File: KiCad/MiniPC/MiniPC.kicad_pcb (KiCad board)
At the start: 2 copper layers, 65 x 30 mm, 5 parts, among them J1 GPIO

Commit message: KiCad 15.05
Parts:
- added C2: 10u, Capacitor_THT:CP_Radial_D5.0mm_P2.00mm, B.Cu at (352.9, 88.5)
- added C3: 100n, Capacitor_THT:C_Disc_D3.0mm_W1.6mm_P2.50mm, B.Cu at (304.3, 57.0)
- added C4: 100n, Capacitor_THT:C_Disc_D3.0mm_W1.6mm_P2.50mm, B.Cu at (304.3, 60.2)
- added C5: 100n, Capacitor_THT:C_Disc_D3.0mm_W1.6mm_P2.50mm, B.Cu at (304.3, 63.4)
- added C6: 100n, Capacitor_THT:C_Disc_D3.0mm_W1.6mm_P2.50mm, B.Cu at (304.3, 66.5)
- added D1: 1N914, Diode_THT:D_DO-41_SOD81_P7.62mm_Horizontal, B.Cu at (376.7, 57.6)
- added D10: 1N914, Diode_THT:D_DO-41_SOD81_P7.62mm_Horizontal, B.Cu at (365.4, 66.1)
- added D11: 1N914, Diode_THT:D_DO-41_SOD81_P7.62mm_Horizontal, B.Cu at (365.4, 70.3)
- added D12: 1N914, Diode_THT:D_DO-41_SOD81_P7.62mm_Horizontal, B.Cu at (365.4, 74.6)
- added D13: 1N914, Diode_THT:D_DO-41_SOD81_P7.62mm_Horizontal, B.Cu at (365.4, 78.8)
- added D14: 1N914, Diode_THT:D_DO-41_SOD81_P7.62mm_Horizontal, B.Cu at (365.4, 83.1)
- added D15: 1N914, Diode_THT:D_DO-41_SOD81_P7.62mm_Horizontal, B.Cu at (354.0, 57.6)
- added D16: 1N914, Diode_THT:D_DO-41_SOD81_P7.62mm_Horizontal, B.Cu at (354.0, 61.9)
- added D17: 1N914, Diode_THT:D_DO-41_SOD81_P7.62mm_Horizontal, B.Cu at (354.0, 66.1)
- added D18: 1N914, Diode_THT:D_DO-41_SOD81_P7.62mm_Horizontal, B.Cu at (354.0, 70.3)
- added D19: 1N914, Diode_THT:D_DO-41_SOD81_P7.62mm_Horizontal, B.Cu at (354.0, 74.6)
- added D2: 1N914, Diode_THT:D_DO-41_SOD81_P7.62mm_Horizontal, B.Cu at (376.7, 61.9)
- added D20: 1N914, Diode_THT:D_DO-41_SOD81_P7.62mm_Horizontal, B.Cu at (354.0, 78.8)
- added D21: 1N914, Diode_THT:D_DO-41_SOD81_P7.62mm_Horizontal, B.Cu at (354.0, 83.1)
- added D22: 1N914, Diode_THT:D_DO-35_SOD27_P7.62mm_Horizontal, B.Cu at (377.0, 87.0)
- added D3: 1N914, Diode_THT:D_DO-41_SOD81_P7.62mm_Horizontal, B.Cu at (376.7, 66.1)
- added D4: 1N914, Diode_THT:D_DO-41_SOD81_P7.62mm_Horizontal, B.Cu at (376.7, 70.3)
- added D5: 1N914, Diode_THT:D_DO-41_SOD81_P7.62mm_Horizontal, B.Cu at (376.7, 74.6)
- added D6: 1N914, Diode_THT:D_DO-41_SOD81_P7.62mm_Horizontal, B.Cu at (376.7, 78.8)
- added D7: 1N914, Diode_THT:D_DO-41_SOD81_P7.62mm_Horizontal, B.Cu at (376.7, 83.1)
- added D8: 1N914, Diode_THT:D_DO-41_SOD81_P7.62mm_Horizontal, B.Cu at (365.4, 57.6)
- added D9: 1N914, Diode_THT:D_DO-41_SOD81_P7.62mm_Horizontal, B.Cu at (365.4, 61.9)
- added J2: Screw_Terminal_01x02, TerminalBlock_Phoenix:TerminalBlock_Phoenix_PT-1,5-2-3.5-H_1x02_P3.50mm_Horizontal, B.Cu at (126.8, 85.2)
- added J3: Conn_01x02_Pin, Connector_PinSocket_2.54mm:PinSocket_1x02_P2.54mm_Vertical, B.Cu at (357.5, 87.5)
- added J4: Screw_Terminal_01x02, TerminalBlock_Phoenix:TerminalBlock_Phoenix_PT-1,5-2-3.5-H_1x02_P3.50mm_Horizontal, B.Cu at (117.7, 85.2)
- added Q1: IRLZ44N, Package_TO_SOT_THT:TO-220-3_Vertical, B.Cu at (316.9, 44.6)
- added R1: 240, Resistor_THT:R_Axial_DIN0204_L3.6mm_D1.6mm_P5.08mm_Horizontal, B.Cu at (366.4, 86.8)
- added R2: 1k, Resistor_THT:R_Axial_DIN0204_L3.6mm_D1.6mm_P5.08mm_Horizontal, B.Cu at (366.4, 90.0)
- added R3: 1k, Resistor_THT:R_Axial_DIN0204_L3.6mm_D1.6mm_P5.08mm_Horizontal, B.Cu at (366.4, 93.1)
- added SW1: SW_Push_45deg, Button_Switch_Keyboard:SW_Cherry_MX_1.00u_Plate, F.Cu at (204.1, 98.5)
- added SW10: SW_Push_45deg, Button_Switch_THT:SW_PUSH_6mm, F.Cu at (237.2, 160.7)
- added SW11: SW_Push_45deg, Button_Switch_THT:SW_PUSH-12mm, F.Cu at (261.4, 101.3)
- added SW12: SW_Push_45deg, Button_Switch_THT:SW_PUSH-12mm, F.Cu at (244.9, 116.5)
- added SW13: SW_Push_45deg, Button_Switch_THT:SW_PUSH_6mm, F.Cu at (237.2, 169.2)
- added SW14: SW_Push_45deg, Button_Switch_THT:SW_PUSH-12mm, F.Cu at (279.2, 116.5)
- added SW15: SW_Push_45deg, Button_Switch_THT:SW_PUSH-12mm, F.Cu at (261.4, 133.1)
- added SW16: SW_Push_45deg, Button_Switch_THT:SW_PUSH_1P1T_6x3.5mm_H5.0_APEM_MJTP1250, F.Cu at (248.4, 82.2)
- added SW17: SW_Push_45deg, Button_Switch_THT:SW_PUSH_1P1T_6x3.5mm_H5.0_APEM_MJTP1250, F.Cu at (261.1, 82.2)
- added SW18: SW_Push_45deg, Button_Switch_THT:SW_PUSH_1P1T_6x3.5mm_H5.0_APEM_MJTP1250, F.Cu at (273.8, 82.2)
- added SW19: SW_SPDT, Button_Switch_THT:SW_DIP_SPSTx01_Slide_9.78x4.72mm_W7.62mm_P2.54mm, B.Cu at (96.5, 72.7)
- added SW2: SW_Push_45deg, Button_Switch_Keyboard:SW_Cherry_MX_1.00u_Plate, F.Cu at (204.1, 113.5)
- added SW20: SW_Push_45deg, Button_Switch_Keyboard:SW_Cherry_MX_1.00u_Plate, F.Cu at (189.1, 98.5)
- added SW21: SW_Push_45deg, Button_Switch_Keyboard:SW_Cherry_MX_1.00u_Plate, F.Cu at (189.1, 113.5)
- added SW22: SW_Push_45deg, Button_Switch_Keyboard:SW_Cherry_MX_1.00u_Plate, F.Cu at (189.1, 128.6)
- added SW3: SW_Push_45deg, Button_Switch_Keyboard:SW_Cherry_MX_1.00u_Plate, F.Cu at (204.1, 128.6)
- added SW4: SW_Push_45deg, Button_Switch_Keyboard:SW_Cherry_MX_1.00u_Plate, F.Cu at (219.2, 98.5)
- added SW5: SW_Push_45deg, Button_Switch_Keyboard:SW_Cherry_MX_1.00u_Plate, F.Cu at (219.2, 113.5)
- added SW6: SW_Push_45deg, Button_Switch_Keyboard:SW_Cherry_MX_1.00u_Plate, F.Cu at (219.2, 128.6)
- added SW7: SW_Push_45deg, Button_Switch_Keyboard:SW_Cherry_MX_1.00u_Plate, F.Cu at (234.3, 98.5)
- added SW8: SW_Push_45deg, Button_Switch_Keyboard:SW_Cherry_MX_1.00u_Plate, F.Cu at (234.3, 113.5)
- added SW9: SW_Push_45deg, Button_Switch_Keyboard:SW_Cherry_MX_1.00u_Plate, F.Cu at (234.3, 128.6)
- added U1: DFRobot DFR0647, MiniPC_Library:DFRobot DFR0647, F.Cu at (209.1, 82.0)
- added U2: COM-09426, MiniPC_Library:COM-09426, F.Cu at (155.9, 114.0)
- added U3: S13V30F5, MiniPC_Library:S13V30F5, B.Cu at (103.8, 44.1)
- added U5: MCP3008, Package_DIP:DIP-16_W7.62mm, B.Cu at (77.6, 40.3)
- added U7: TP4056, MiniPC_Library:TP4056, B.Cu at (152.2, 48.2)
- moved J1 76.9 mm to (184.9, 67.3)
- moved MH1 76.9 mm to (180.1, 66.0)
- moved MH2 76.9 mm to (238.1, 66.0)
- moved MH3 76.9 mm to (180.1, 89.0)
- moved MH4 76.9 mm to (238.1, 89.0)
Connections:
- net GND renamed GNDA
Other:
- board outline removed
- board text removed: "PoE"

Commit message: KiCad 16.05
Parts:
- SW10, SW13: moved to B.Cu
- SW19: moved to F.Cu
- moved R1 225.8 mm to (140.6, 93.7), turned to -90 degrees
- moved R2 223.4 mm to (143.2, 98.7), turned to 90 degrees
- moved D10 208.0 mm to (157.4, 59.4)
- moved D7 192.2 mm to (191.4, 134.3), turned to -90 degrees
- moved D4 190.7 mm to (191.4, 115.2), turned to -90 degrees
- moved D1 189.3 mm to (191.4, 96.2), turned to -90 degrees
- moved D21 188.7 mm to (172.4, 134.3), turned to -90 degrees
- moved C2 185.3 mm to (168.6, 69.4), turned to 90 degrees
- moved D20 185.2 mm to (172.4, 115.2), turned to -90 degrees
- moved D19 182.9 mm to (172.4, 96.2), turned to -90 degrees
- moved D8 172.8 mm to (210.5, 134.3), turned to -90 degrees
- moved C4 172.7 mm to (140.6, 115.2), turned to 90 degrees
- moved D5 171.1 mm to (210.5, 115.2), turned to -90 degrees
- moved D2 169.8 mm to (210.5, 96.2), turned to -90 degrees
- moved D9 153.9 mm to (229.5, 134.3), turned to -90 degrees
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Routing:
- net /GPIO25: track 0.00 -> 57.2 mm
- net /GPIO24: track 0.00 -> 57.2 mm
- net /GPIO23: track 0.00 -> 57.2 mm
- net /ID_SDA: track 0.00 -> 38.1 mm
- net /GPIO6: track 0.00 -> 38.1 mm
- net /GPIO5: track 0.00 -> 38.1 mm
- net /GPIO22: track 0.00 -> 38.1 mm
- net Net-(D9-A): track 0.00 -> 5.53 mm
- net Net-(D8-A): track 0.00 -> 5.53 mm
- net Net-(D7-A): track 0.00 -> 5.53 mm
- net Net-(D6-A): track 0.00 -> 5.53 mm
- net Net-(D5-A): track 0.00 -> 5.53 mm
- net Net-(D4-A): track 0.00 -> 5.53 mm
- net Net-(D3-A): track 0.00 -> 5.53 mm
- net Net-(D21-A): track 0.00 -> 5.53 mm
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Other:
- board outline added: 160 x 105 mm

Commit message: KiCad 17.05
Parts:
- added REF**: MountingHole_2.2mm_M2, MountingHole:MountingHole_2.2mm_M2, F.Cu at (190.7, 81.0)
- added REF**: MountingHole_2.5mm, MountingHole:MountingHole_2.5mm, F.Cu at (196.9, 92.3)
- added REF**: MountingHole_2mm, MountingHole:MountingHole_2mm, F.Cu at (144.7, 127.2)
- added REF**: MountingHole_2mm, MountingHole:MountingHole_2mm, F.Cu at (144.7, 145.8)
- added REF**: MountingHole_2.2mm_M2, MountingHole:MountingHole_2.2mm_M2, F.Cu at (190.7, 73.0)
- added REF**: MountingHole_2.2mm_M2, MountingHole:MountingHole_2.2mm_M2, F.Cu at (227.6, 73.0)
- added REF**: MountingHole_2.5mm, MountingHole:MountingHole_2.5mm, F.Cu at (223.3, 65.8)
- added REF**: MountingHole_2mm, MountingHole:MountingHole_2mm, F.Cu at (163.9, 122.0)
- added REF**: MountingHole_2.5mm, MountingHole:MountingHole_2.5mm, F.Cu at (223.3, 92.3)
- added REF**: MountingHole_2mm, MountingHole:MountingHole_2mm, F.Cu at (143.8, 123.0)
- added REF**: MountingHole_2.5mm, MountingHole:MountingHole_2.5mm, F.Cu at (196.9, 65.9)
- added REF**: MountingHole_2.2mm_M2, MountingHole:MountingHole_2.2mm_M2, F.Cu at (227.6, 81.0)
- moved SW15 22.3 mm to (283.0, 112.0)
- moved SW14 22.3 mm to (267.2, 96.3)
- moved SW12 22.3 mm to (267.2, 127.8)
- moved SW11 22.3 mm to (251.5, 112.0)
- moved J4 18.0 mm to (154.2, 151.5)
- moved U3 17.5 mm to (152.4, 136.0), turned to 90 degrees
- moved D11 6.35 mm to (246.1, 124.1)
- moved D14 6.35 mm to (246.1, 130.5)
- moved J1 5.00 mm to (184.9, 62.3)
- moved C3 5.00 mm to (186.4, 78.5)
- moved MH3 5.00 mm to (180.1, 84.0)
- moved MH4 5.00 mm to (238.1, 84.0)
- moved U1 5.00 mm to (209.1, 77.0)
- moved MH1 5.00 mm to (180.1, 61.0)
- moved MH2 5.00 mm to (238.1, 61.0)
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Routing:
- net GNDA: track 0.00 -> 302.4 mm
- net /GPIO23: track 57.2 -> 257.5 mm
- net /GPIO13/PWM1: track 0.00 -> 197.8 mm
- net /GPIO18/PCM.CLK: track 0.00 -> 189.0 mm
- net +5V: track 0.00 -> 166.2 mm
- net /GPIO24: track 57.2 -> 220.0 mm
- net /GPIO25: track 57.2 -> 202.3 mm
- net /GPIO19/PCM.FS: track 0.00 -> 140.5 mm
- net +3V3: track 0.00 -> 98.3 mm
- net Net-(SW19-B): track 0.00 -> 88.9 mm
- net /GPIO11/SPI0.SCLK: track 0.00 -> 68.8 mm
- net /GPIO10/SPI0.MOSI: track 0.00 -> 67.6 mm
- net /GPIO9/SPI0.MISO: track 0.00 -> 66.9 mm
- net /GPIO26: track 0.00 -> 63.4 mm
- net Net-(D15-A): track 0.00 -> 57.1 mm
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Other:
- copper layers 2 -> 4

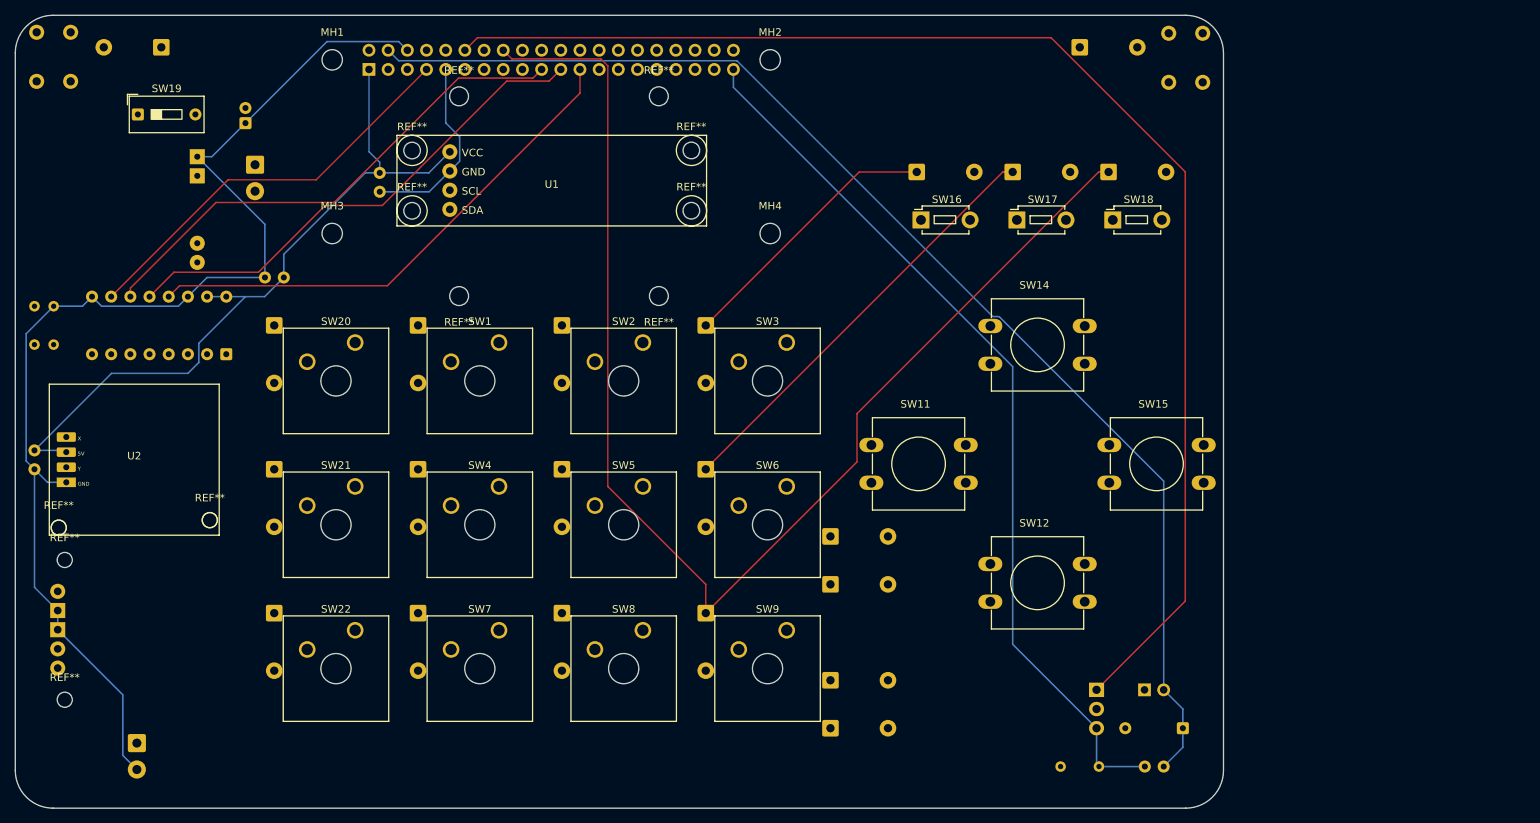
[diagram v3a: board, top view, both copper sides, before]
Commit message: Ki-Cad 30.05
Zmiana na Raspberry Pi 5
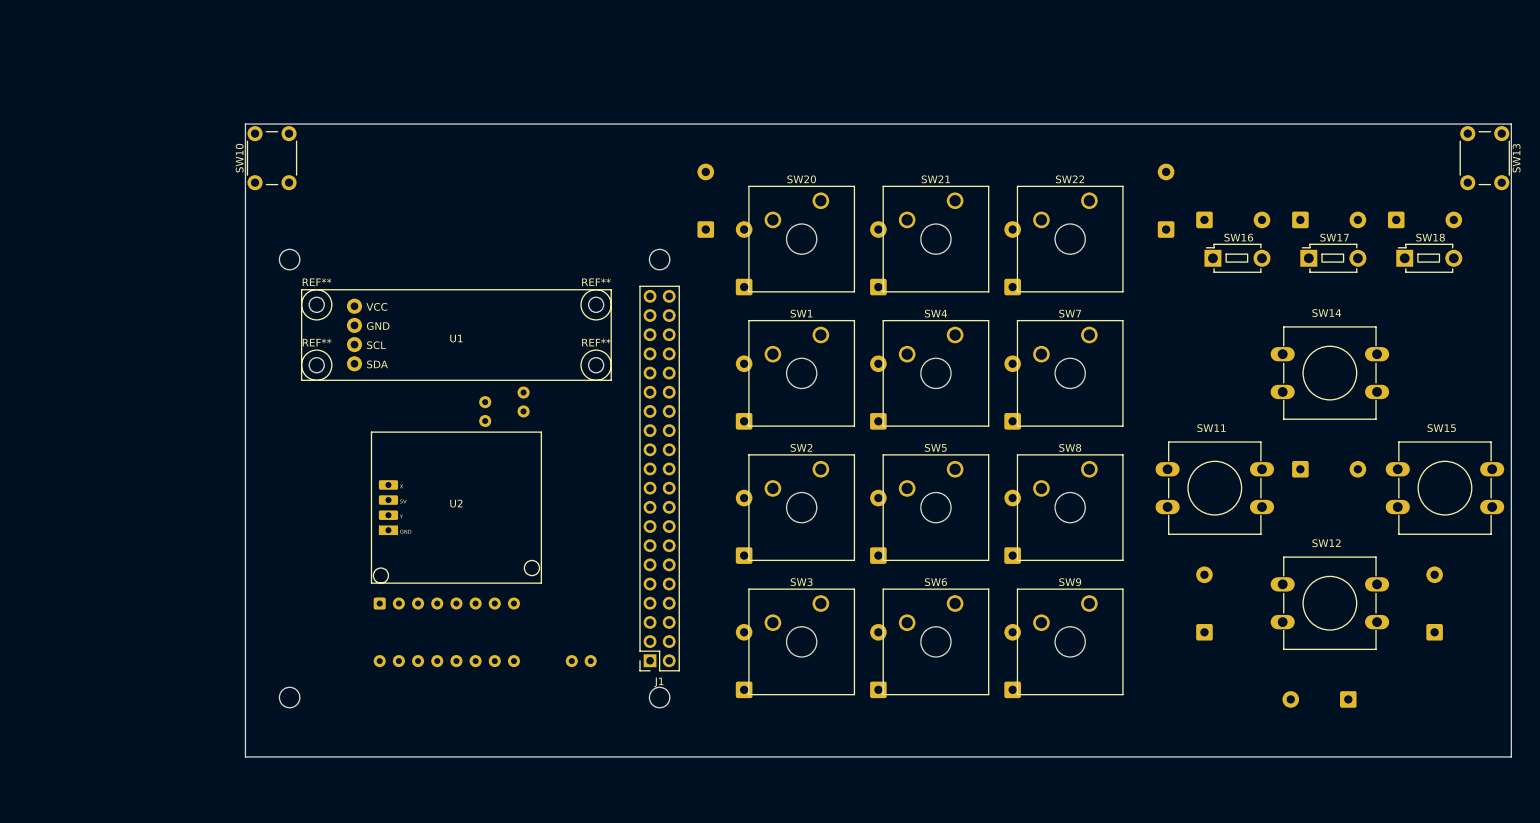
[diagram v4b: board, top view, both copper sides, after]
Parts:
- removed C2: 10u, Capacitor_THT:CP_Radial_D5.0mm_P2.00mm
- removed C6: 100n, Capacitor_THT:C_Disc_D3.0mm_W1.6mm_P2.50mm
- removed D22: 1N914, Diode_THT:D_DO-35_SOD27_P7.62mm_Horizontal
- removed J2, J4: Screw_Terminal_01x02, TerminalBlock_Phoenix:TerminalBlock_Phoenix_PT-1,5-2-3.5-H_1x02_P3.50mm_Horizontal
- removed J3: Conn_01x02_Pin, Connector_PinSocket_2.54mm:PinSocket_1x02_P2.54mm_Vertical
- removed Q1: IRLZ44N, Package_TO_SOT_THT:TO-220-3_Vertical
- removed R1: 240, Resistor_THT:R_Axial_DIN0204_L3.6mm_D1.6mm_P5.08mm_Horizontal
- removed R2, R3: 1k, Resistor_THT:R_Axial_DIN0204_L3.6mm_D1.6mm_P5.08mm_Horizontal
- removed the REF** at (190.7, 81.0)
- removed the REF** at (196.9, 92.3)
- removed the REF** at (144.7, 127.2)
- removed the REF** at (144.7, 145.8)
- removed the REF** at (190.7, 73.0)
- removed the REF** at (227.6, 73.0)
- removed the REF** at (223.3, 65.8)
- removed the REF** at (163.9, 122.0)
- removed the REF** at (223.3, 92.3)
- removed the REF** at (143.8, 123.0)
- removed the REF** at (196.9, 65.9)
- removed the REF** at (227.6, 81.0)
- removed SW19: SW_SPDT, Button_Switch_THT:SW_DIP_SPSTx01_Slide_9.78x4.72mm_W7.62mm_P2.54mm
- removed U3: S13V30F5, MiniPC_Library:S13V30F5
- removed U7: TP4056, MiniPC_Library:TP4056
- added REF**: MountingHole_2mm, MountingHole:MountingHole_2mm, F.Cu at (178.0, 101.5)
- added REF**: MountingHole_2mm, MountingHole:MountingHole_2mm, F.Cu at (178.0, 93.5)
- added REF**: MountingHole_2mm, MountingHole:MountingHole_2mm, F.Cu at (215.0, 101.5)
- added REF**: MountingHole_2mm, MountingHole:MountingHole_2mm, F.Cu at (215.0, 93.5)
- J1, SW10, SW13: moved to F.Cu
- MH1, MH2, MH3, MH4: moved to B.Cu
- moved SW22 112.6 mm to (280.3, 79.7)
- moved D21 106.9 mm to (270.2, 91.1), turned to 90 degrees
- moved MH1 94.9 mm to (223.4, 145.5), turned to 90 degrees
- moved SW21 88.0 mm to (262.6, 79.7)
- moved SW7 87.4 mm to (280.3, 97.5)
- moved J1 86.7 mm to (222.2, 140.6), turned to 180 degrees
- moved D20 83.6 mm to (252.4, 91.1), turned to 90 degrees
- moved D7 82.7 mm to (270.2, 108.9), turned to 90 degrees
- moved D15 81.0 mm to (326.1, 136.8), turned to 90 degrees
- moved D10 76.0 mm to (229.5, 83.5), turned to 90 degrees
- moved D12 68.6 mm to (314.6, 145.7), turned to 180 degrees
- moved C5 65.1 mm to (211.8, 140.6)
- moved SW20 64.5 mm to (244.8, 79.7)
- moved D14 64.1 mm to (308.3, 115.2)
- moved MH4 63.7 mm to (174.4, 87.5), turned to 90 degrees
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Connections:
- U2 pad 1: /X -> Net-(U2-X)
- U2 pad 3: /Y -> Net-(U2-Y)
- U5 pad 1: Net-(U5-CH0) -> unconnected-(U5-CH0-Pad1)
- U5 pad 2: /Y -> Net-(U2-X)
- U5 pad 3: /X -> Net-(U2-Y)
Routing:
- net GNDA: track 302.4 -> 0.00 mm
- net /GPIO23: track 257.5 -> 0.00 mm
- net /GPIO24: track 220.0 -> 0.00 mm
- net /GPIO25: track 202.3 -> 0.00 mm
- net /GPIO13/PWM1: track 197.8 -> 0.00 mm
- net /GPIO18/PCM.CLK: track 189.0 -> 0.00 mm
- net +5V: track 166.2 -> 0.00 mm
- net /GPIO19/PCM.FS: track 140.5 -> 0.00 mm
- net +3V3: track 98.3 -> 0.00 mm
- net Net-(SW19-B): track 88.9 -> 0.00 mm
- net /GPIO22: track 82.4 -> 0.00 mm
- net /GPIO6: track 81.4 -> 0.00 mm
- net /ID_SDA: track 80.8 -> 0.00 mm
- net /GPIO5: track 75.5 -> 0.00 mm
- net /GPIO11/SPI0.SCLK: track 68.8 -> 0.00 mm
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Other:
- board size 160 x 105 mm -> 167.6 x 83.8 mm
- board text added: "PoE"
- board text added: "RJ45"
- board text added: "USB"

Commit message: KiCad v2 05.06
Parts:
- removed U2: COM-09426, MiniPC_Library:COM-09426
- added U3: Adafruit 5628, MiniPC_Library:P5628_C17894, F.Cu at (190.1, 119.2)
- moved C3 16.7 mm to (188.9, 107.6), turned to 90 degrees
- moved C4 16.7 mm to (214.3, 115.4)
- moved U5 2.54 mm to (188.9, 133.0)
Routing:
- net /GPIO24: track 0.00 -> 251.4 mm
- net /GPIO23: track 0.00 -> 249.9 mm
- net /GPIO13/PWM1: track 0.00 -> 184.9 mm
- net /GPIO25: track 0.00 -> 179.5 mm
- net /GPIO19/PCM.FS: track 0.00 -> 167.5 mm
- net +3V3: track 0.00 -> 113.0 mm
- net /GPIO26: track 0.00 -> 107.6 mm
- net /GPIO22: track 0.00 -> 103.0 mm
- net GNDA: track 0.00 -> 101.3 mm
- net /GPIO6: track 0.00 -> 78.1 mm
- net /GPIO2/SDA1: track 0.00 -> 69.5 mm
- net /GPIO3/SCL1: track 0.00 -> 67.4 mm
- net /GPIO5: track 0.00 -> 65.8 mm
- net /ID_SDA: track 0.00 -> 62.4 mm
- net Net-(D10-A): track 0.00 -> 62.3 mm
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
